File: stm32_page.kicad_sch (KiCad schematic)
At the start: 1 part, among them U1 STM32L431KBU6_C2826408

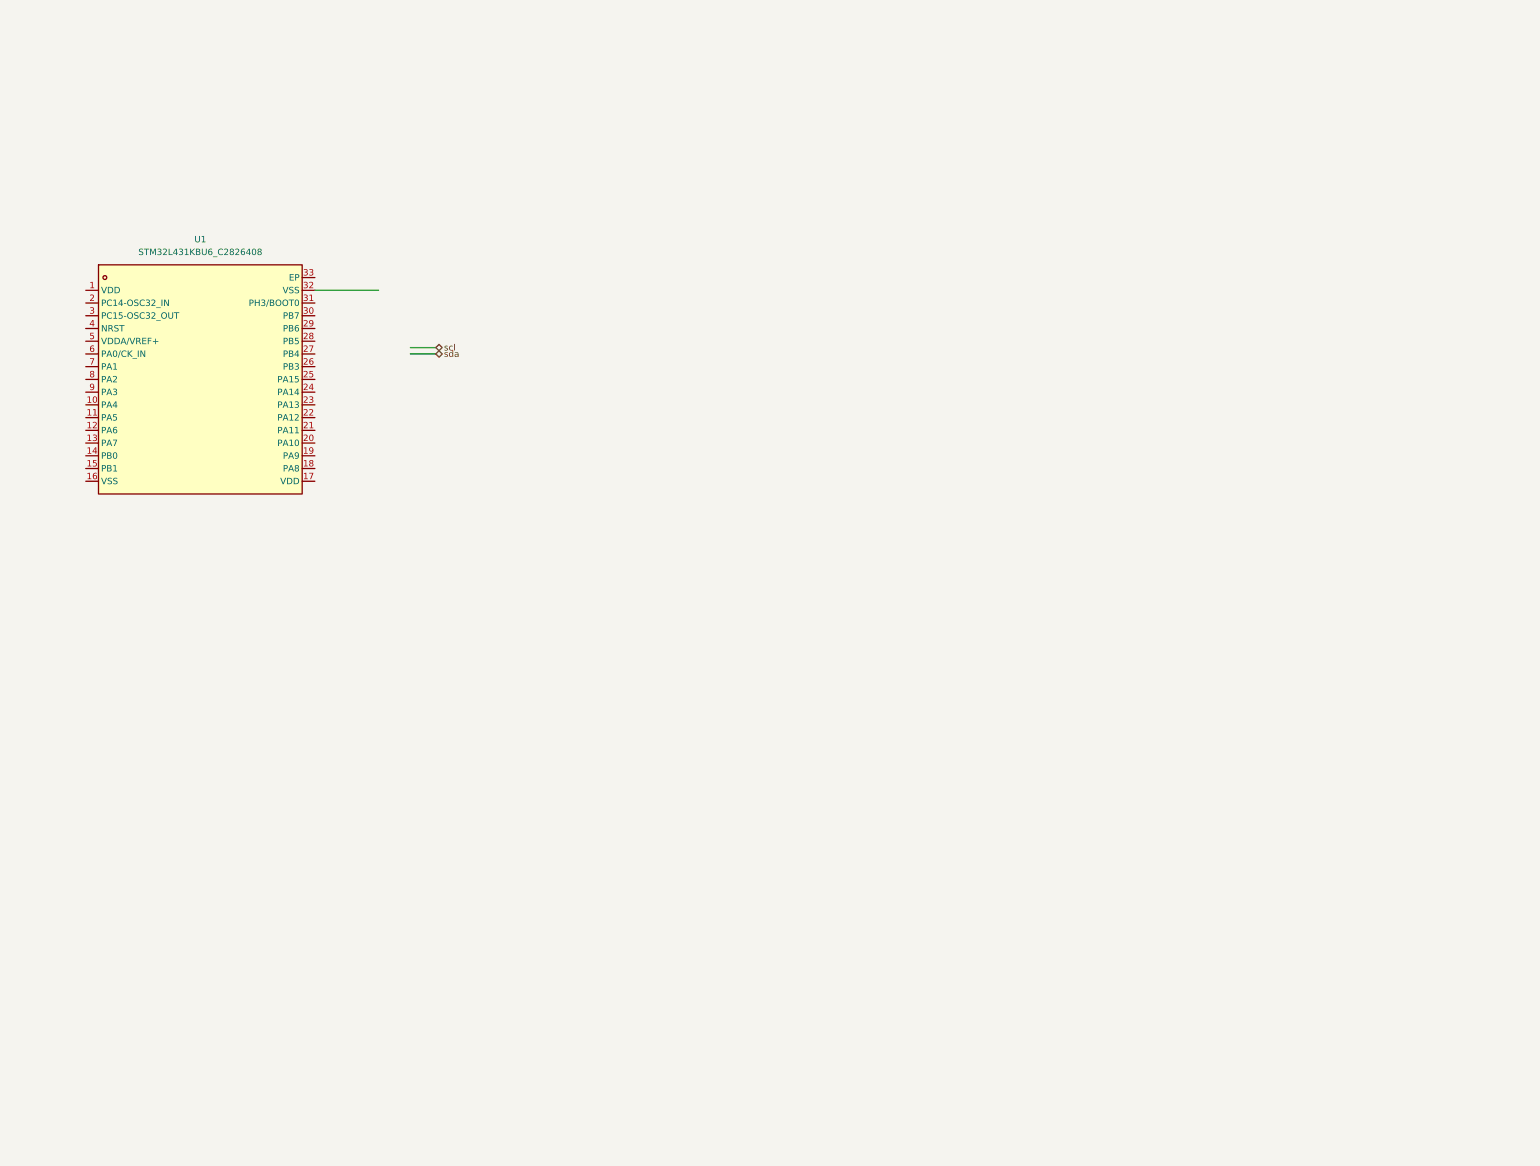
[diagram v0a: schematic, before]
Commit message: adding jtag and power cap
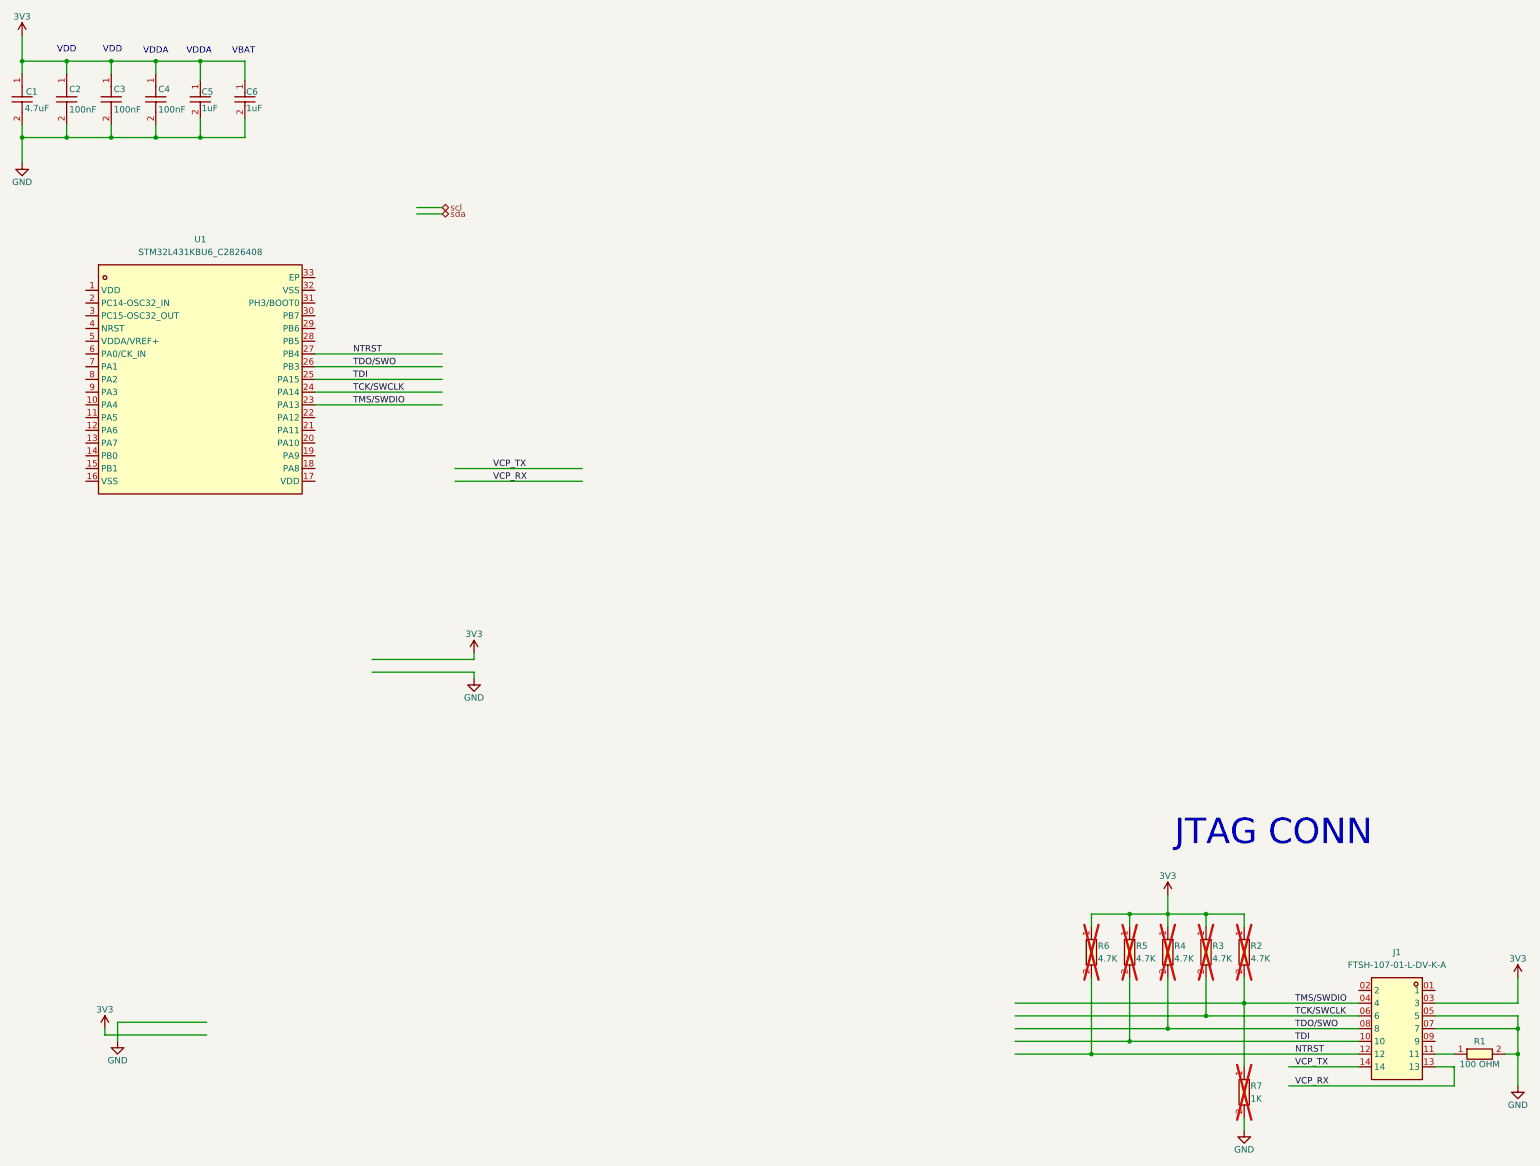
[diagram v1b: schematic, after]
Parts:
- added C1: CL05A475MO5NUNC, easyeda2kicad:C0402, symbol easyeda2kicad:CL05A475MO5NUNC
- added C2, C3, C4: CC0402JRX7R7BB104, easyeda2kicad:C0402, symbol easyeda2kicad:CC0402JRX7R7BB104
- added C5, C6: CL10B105KA8NNNC, easyeda2kicad:C0603, symbol easyeda2kicad:CL10B105KA8NNNC
- added J1: FTSH-107-01-L-DV-K-A, easyeda2kicad:HDR-SMD_14P-P1.27_FTSH-107-01-L-DV-K-A, symbol easyeda2kicad:FTSH-107-01-L-DV-K-A
- added R1: 0402WGF1000TCE, easyeda2kicad:R0402, symbol easyeda2kicad:0402WGF1000TCE
- added R2, R3, R4, R5, R6: 0402WGF4701TCE, easyeda2kicad:R0402, symbol easyeda2kicad:0402WGF4701TCE
- added R7: 0402WGF1001TCE, easyeda2kicad:R0402, symbol easyeda2kicad:0402WGF1001TCE
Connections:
- net TMS/SWDIO: now reaches U1.23 (PA13)
- net TMS/SWDIO: now also J1.04 (4), R2.2, R7.1
- net TCK/SWCLK: now reaches U1.24 (PA14)
- net TCK/SWCLK: now also J1.06 (6), R3.2
- net TDI: now reaches U1.25 (PA15)
- net TDI: now also J1.10, R5.2
- net TDO/SWO: now reaches U1.26 (PB3)
- net TDO/SWO: now also J1.08 (8), R4.2
- net NTRST: now reaches U1.27 (PB4)
- net NTRST: now also J1.12, R6.2
- new net: J1.11, R1.1
- new net 3V3: C1.1, C2.1, C3.1, C4.1, C5.1, C6.1, J1.03 (3), R2.1, R3.1, R4.1, R5.1, R6.1
- new net GND: C1.2, C2.2, C3.2, C4.2, C5.2, C6.2, J1.05 (5), J1.07 (7), R1.2, R7.2
- new net VCP_RX: J1.13
- new net VCP_TX: J1.14
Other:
- note added: "JTAG CONN"
- note added: "VBAT"
- note added: "VDD"
- note added: "VDDA"

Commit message: updating res and cap to 0603, adding OSC32 DRP, JTAG done, power done
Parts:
- removed C1: CL05A475MO5NUNC, easyeda2kicad:C0402, symbol easyeda2kicad:CL05A475MO5NUNC
- removed C2, C3, C4: CC0402JRX7R7BB104, easyeda2kicad:C0402, symbol easyeda2kicad:CC0402JRX7R7BB104
- removed C5, C6: CL10B105KA8NNNC, easyeda2kicad:C0603, symbol easyeda2kicad:CL10B105KA8NNNC
- removed R1: 0402WGF1000TCE, easyeda2kicad:R0402, symbol easyeda2kicad:0402WGF1000TCE
- removed R2, R3, R4, R5, R6: 0402WGF4701TCE, easyeda2kicad:R0402, symbol easyeda2kicad:0402WGF4701TCE
- removed R7: 0402WGF1001TCE, easyeda2kicad:R0402, symbol easyeda2kicad:0402WGF1001TCE
- added C1: CL10A475KO8NNNC, easyeda2kicad:C0603, symbol easyeda2kicad:CL10A475KO8NNNC
- added C2, C4: CL10B104KO8NNNC, easyeda2kicad:C0603, symbol easyeda2kicad:CL10B104KO8NNNC
- added C5, C6: CL10A105KO8NNNC, easyeda2kicad:C0603, symbol easyeda2kicad:CL10A105KO8NNNC
- added C7, C8: 0603CG7R0C500NT, easyeda2kicad:C0603, symbol easyeda2kicad:0603CG7R0C500NT
- added R1: 0603WAF1000T5E, easyeda2kicad:R0603, symbol easyeda2kicad:0603WAF1000T5E
- added R11: 0603WAF1001T5E, easyeda2kicad:R0603, symbol easyeda2kicad:0603WAF1001T5E
- added R2, R3, R4, R5, R6: 0603WAF4701T5E, easyeda2kicad:R0603, symbol easyeda2kicad:0603WAF4701T5E
- added X1: SC-32S32.768kHz20PPM7pF, easyeda2kicad:OSC-SMD_L3.2-W1.5, symbol easyeda2kicad:SC-32S32.768kHz20PPM7pF
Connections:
- net 3V3 is gone; now on net +3V3: J1.03 (3)
- net GND: now also U1.16 (VSS), U1.32 (VSS), C1.2, C2.2, C4.2, C5.2, C6.2, C7.1, C8.1, R1.2, R11.2
- net NTRST: now also R6.2
- net TCK/SWCLK: now also R3.2
- net TDI: now also R5.2
- net TDO/SWO: now also R4.2
- net TMS/SWDIO: now also R11.1, R2.2
- net at J1.11: now also R1.1
- net +3V3: now reaches U1.1 (VDD)
- net +3V3: now also U1.17 (VDD), C1.1, C2.1, C4.1, C5.1, C6.1, R2.1, R3.1, R4.1, R5.1, R6.1
- net OSC32_IN: now reaches U1.2 (PC14-OSC32_IN)
- net OSC32_IN: now also C7.2, X1.1
- net OSC32_OUT: now reaches U1.3 (PC15-OSC32_OUT)
- net OSC32_OUT: now also C8.2, X1.2
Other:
- moved on the sheet: U1

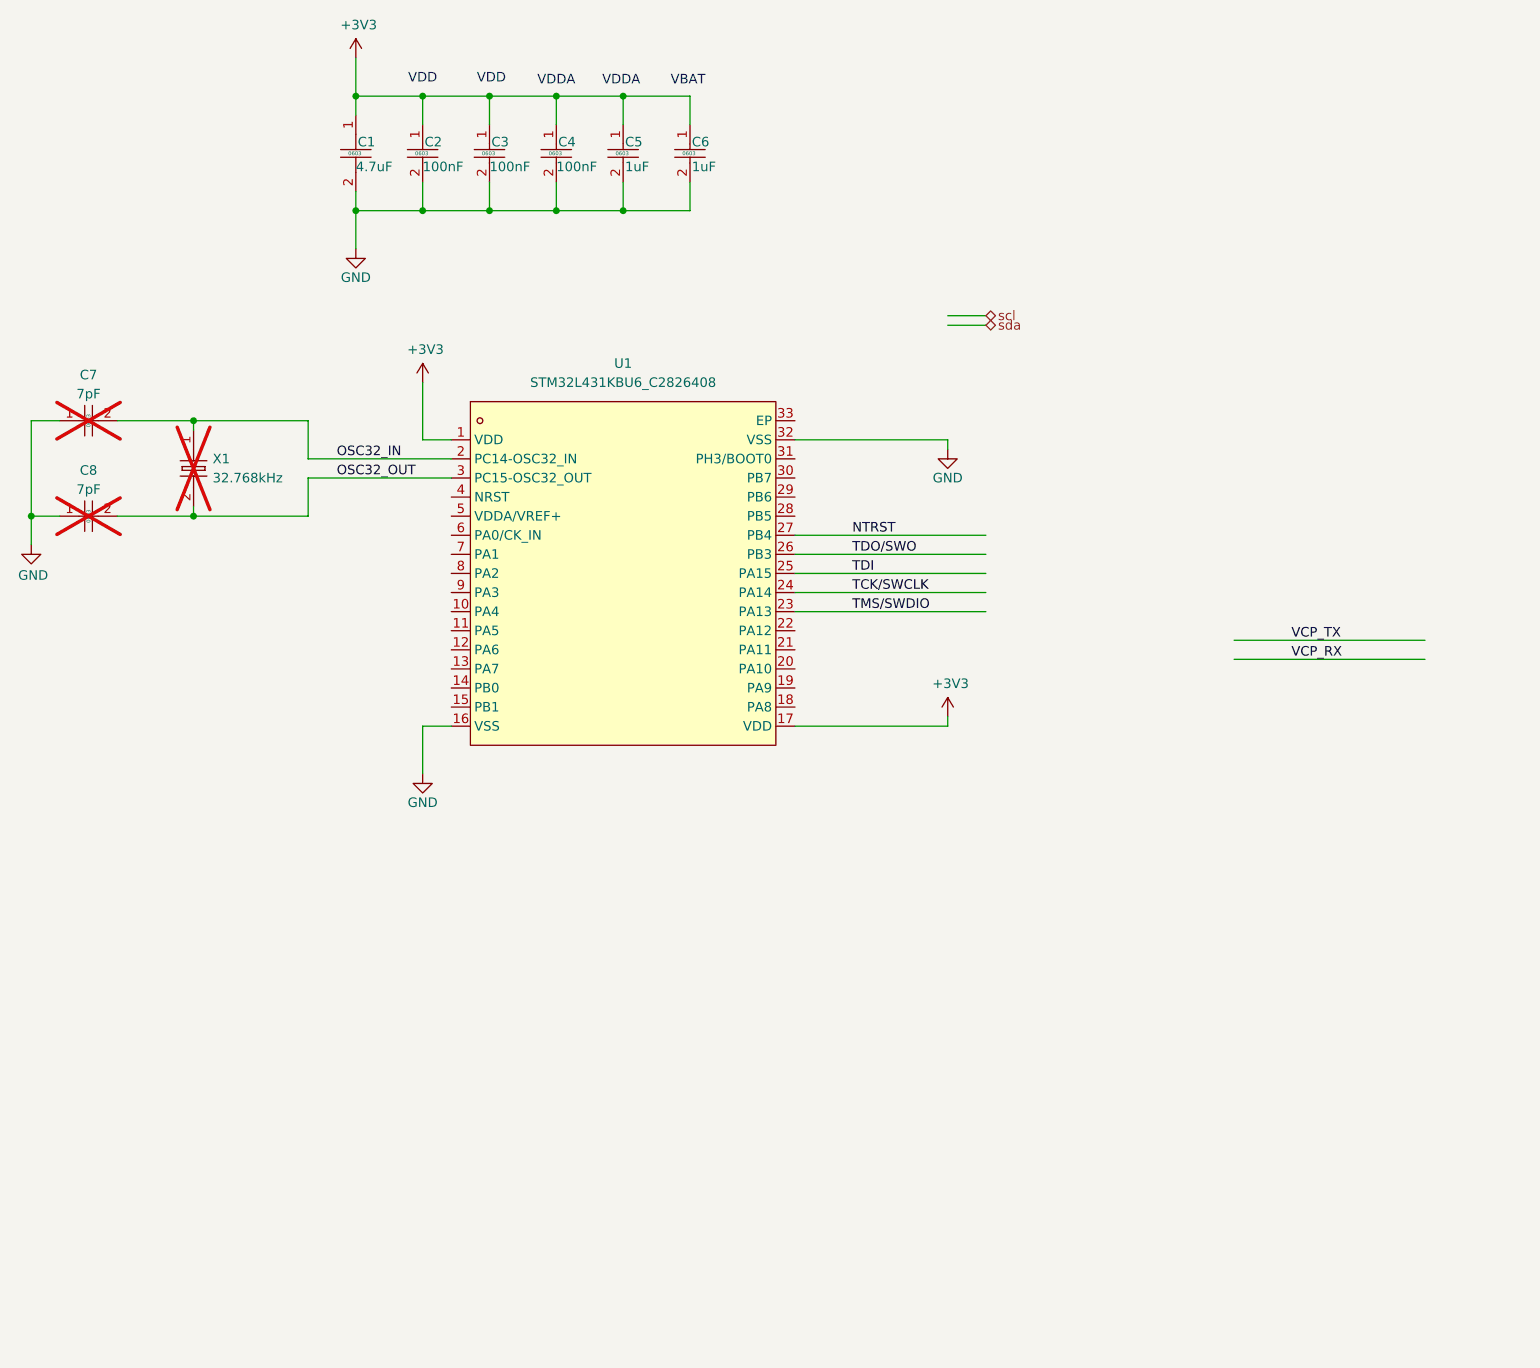
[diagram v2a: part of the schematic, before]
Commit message: Cap updated again to basic parts
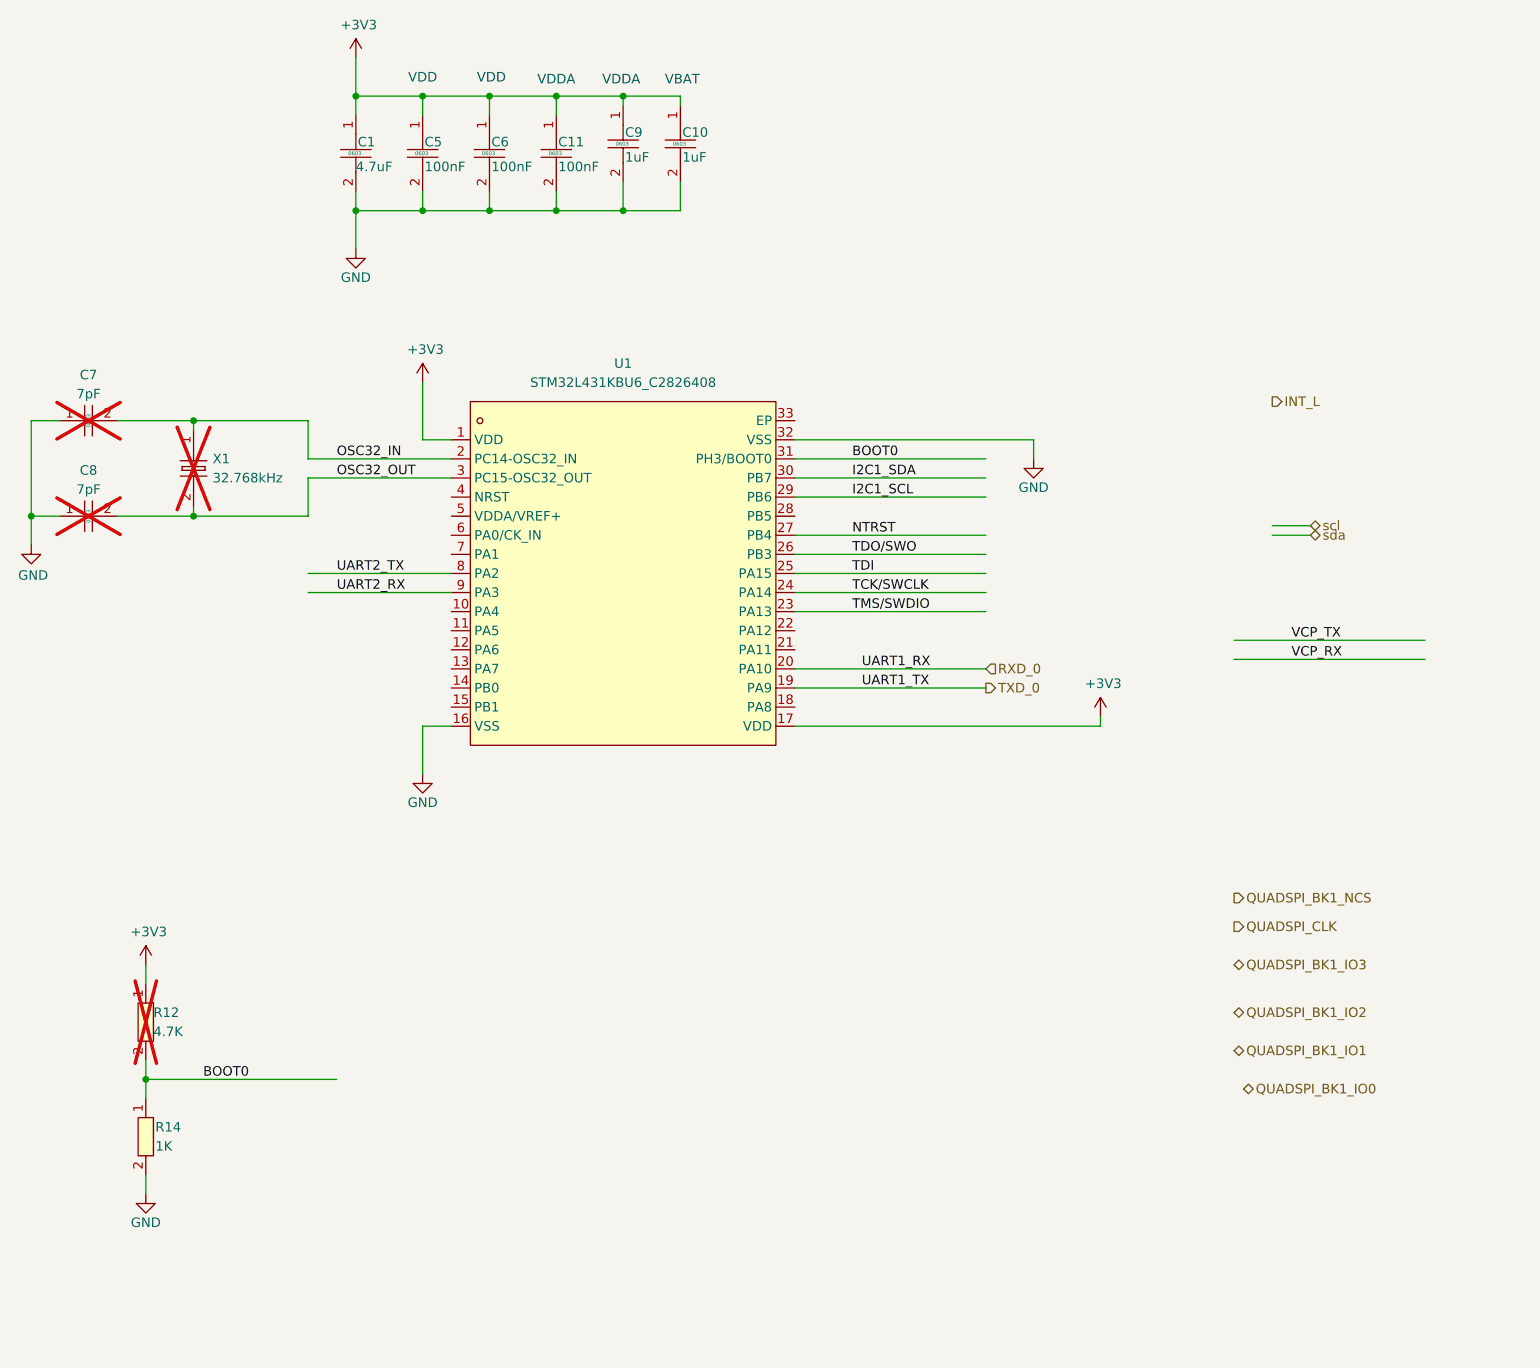
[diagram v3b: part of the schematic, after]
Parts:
- removed C2, C4: CL10B104KO8NNNC, easyeda2kicad:C0603, symbol easyeda2kicad:CL10B104KO8NNNC
- removed C5, C6: CL10A105KO8NNNC, easyeda2kicad:C0603, symbol easyeda2kicad:CL10A105KO8NNNC
- added C10, C9: CL10A105KB8NNNC, easyeda2kicad:C0603, symbol easyeda2kicad:CL10A105KB8NNNC
- added C11, C5, C6: CC0603KRX7R9BB104, easyeda2kicad:C0603, symbol easyeda2kicad:CC0603KRX7R9BB104
- added R12: 0603WAF4701T5E, easyeda2kicad:R0603, symbol easyeda2kicad:0603WAF4701T5E
- added R14: 0603WAF1001T5E, easyeda2kicad:R0603, symbol easyeda2kicad:0603WAF1001T5E
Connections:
- net +3V3: now also C10.1, C11.1, C5.1, C6.1, C9.1, R12.1
- net GND: now also C10.2, C11.2, C5.2, C6.2, C9.2, R14.2
- net TXD_0: now reaches U1.19 (PA9)
- net RXD_0: now reaches U1.20 (PA10)
- net I2C1_SCL: now reaches U1.29 (PB6)
- net I2C1_SDA: now reaches U1.30 (PB7)
- net BOOT0: now reaches U1.31 (PH3/BOOT0)
- net BOOT0: now also R12.2, R14.1
- net UART2_TX: now reaches U1.8 (PA2)
- net UART2_RX: now reaches U1.9 (PA3)
